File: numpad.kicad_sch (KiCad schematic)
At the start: 1 part, among them U1 ATmega328P-P

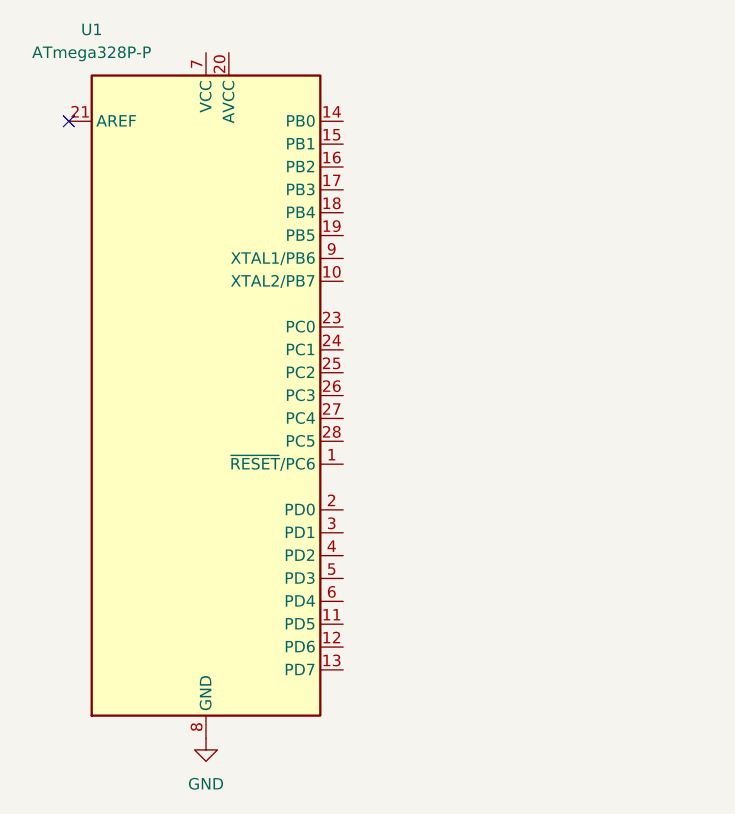
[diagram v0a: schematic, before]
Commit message: 스키메틱에 발진회로 추가
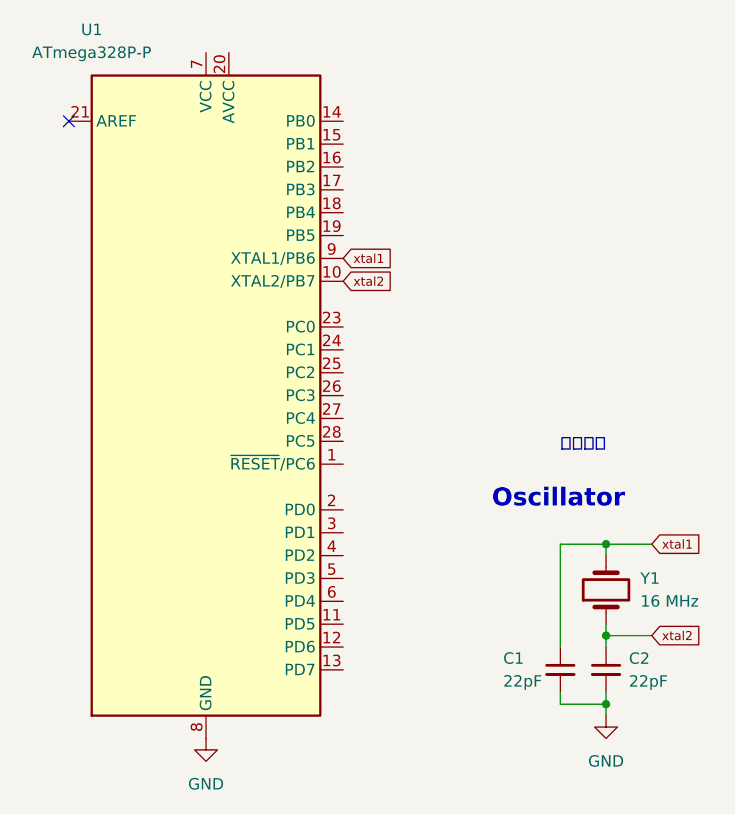
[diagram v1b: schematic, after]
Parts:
- added C1, C2: 22pF, symbol Device:C_Small
- added Y1: 16 MHz, symbol Device:Crystal
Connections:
- net GND: now also C1.2, C2.2
- net xtal2: now reaches U1.10 (XTAL2/PB7)
- net xtal2: now also C2.1, Y1.1
- net xtal1: now reaches U1.9 (XTAL1/PB6)
- net xtal1: now also C1.1, Y1.2
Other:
- note added: "Oscillator"
- note added: "발진회로"
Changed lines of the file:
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@@
 (kicad_sch (version 20211123) (generator eeschema)
   (paper "A4")
+  (junction (at 80.01 165.1) (diameter 0) (color 0 0 0 0)
+  )
+  (junction (at 80.01 182.88) (diameter 0) (color 0 0 0 0)
+  )
+  (junction (at 80.01 175.26) (diameter 0) (color 0 0 0 0)
+  )
   (no_connect (at 20.32 118.11))
+  (wire (pts (xy 85.09 165.1) (xy 80.01 165.1))
+    (stroke (width 0) (type default) (color 0 0 0 0))
+  )
+  (wire (pts (xy 74.93 181.61) (xy 74.93 182.88))
+    (stroke (width 0) (type default) (color 0 0 0 0))
+  )
+  (wire (pts (xy 80.01 165.1) (xy 80.01 166.37))
+    (stroke (width 0) (type default) (color 0 0 0 0))
+  )
+  (wire (pts (xy 80.01 175.26) (xy 85.09 175.26))
+    (stroke (width 0) (type default) (color 0 0 0 0))
+  )
+  (wire (pts (xy 80.01 175.26) (xy 80.01 176.53))
+    (stroke (width 0) (type default) (color 0 0 0 0))
+  )
+  (wire (pts (xy 80.01 182.88) (xy 80.01 184.15))
+    (stroke (width 0) (type default) (color 0 0 0 0))
+  )
+  (wire (pts (xy 74.93 165.1) (xy 74.93 176.53))
+    (stroke (width 0) (type default) (color 0 0 0 0))
+  )
+  (wire (pts (xy 80.01 175.26) (xy 80.01 173.99))
+    (stroke (width 0) (type default) (color 0 0 0 0))
+  )
+  (wire (pts (xy 74.93 165.1) (xy 80.01 165.1))
+    (stroke (width 0) (type default) (color 0 0 0 0))
+  )
+  (wire (pts (xy 80.01 181.61) (xy 80.01 182.88))
+    (stroke (width 0) (type default) (color 0 0 0 0))
+  )
+  (wire (pts (xy 74.93 182.88) (xy 80.01 182.88))
+    (stroke (width 0) (type default) (color 0 0 0 0))
+  )
+  (text "발진회로" (at 74.93 154.94 0)
+    (effects (font (size 1.27 1.27)) (justify left bottom))
+  )
+  (text "Oscillator" (at 67.31 161.29 0)
+    (effects (font (size 2 2) (thickness 0.4) bold) (justify left bottom))
+  )
+  (global_label "xtal2" (shape input) (at 50.8 135.89 0) (fields_autoplaced)
+    (effects (font (size 1 1)) (justify left))
+    (property "Intersheet References" "${INTERSHEET_REFS}" (id 0) (at 56.4619 135.8275 0)
+      (effects (font (size 1 1)) (justify left) hide)
+    )
+  )
+  (global_label "xtal2" (shape input) (at 85.09 175.26 0) (fields_autoplaced)
+    (effects (font (size 1 1)) (justify left))
+    (property "Intersheet References" "${INTERSHEET_REFS}" (id 0) (at 90.7519 175.1975 0)
+      (effects (font (size 1 1)) (justify left) hide)
+    )
+  )
+  (global_label "xtal1" (shape input) (at 85.09 165.1 0) (fields_autoplaced)
+    (effects (font (size 1 1)) (justify left))
+    (property "Intersheet References" "${INTERSHEET_REFS}" (id 0) (at 90.7519 165.0375 0)
+      (effects (font (size 1 1)) (justify left) hide)
+    )
+  )
+  (global_label "xtal1" (shape input) (at 50.8 133.35 0) (fields_autoplaced)
+    (effects (font (size 1 1)) (justify left))
+    (property "Intersheet References" "${INTERSHEET_REFS}" (id 0) (at 56.4619 133.2875 0)
+      (effects (font (size 1 1)) (justify left) hide)
+    )
+  )
+  (symbol (lib_id "Device:C_Small") (at 74.93 179.07 0) (unit 1)
+    (in_bom yes) (on_board yes)
+    (property "Reference" "C1" (id 0) (at 68.58 177.8 0)
+      (effects (font (size 1.27 1.27)) (justify left))
+    )
+    (property "Value" "22pF" (id 1) (at 68.58 180.34 0)
+      (effects (font (size 1.27 1.27)) (justify left))
+    )
+    (property "Footprint" "" (id 2) (at 74.93 179.07 0)
+      (effects (font (size 1.27 1.27)) hide)
+    )
+    (property "Datasheet" "~" (id 3) (at 74.93 179.07 0)
+      (effects (font (size 1.27 1.27)) hide)
+    )
+    (pin "1")
+    (pin "2")
+  )
   (symbol (lib_id "power:GND") (at 35.56 186.69 0) (unit 1)
     (in_bom yes) (on_board yes) (fields_autoplaced)
-    (property "Reference" "#PWR?" (id 0) (at 35.56 193.04 0)
+    (property "Reference" "#PWR01" (id 0) (at 35.56 193.04 0)
       (effects (font (size 1.27 1.27)) hide)
     )
@@
     )
     (property "Datasheet" "" (id 3) (at 35.56 186.69 0)
+      (effects (font (size 1.27 1.27)) hide)
+    )
+    (pin "1")
+  )
+  (symbol (lib_id "Device:C_Small") (at 80.01 179.07 0) (unit 1)
+    (in_bom yes) (on_board yes) (fields_autoplaced)
+    (property "Reference" "C2" (id 0) (at 82.55 177.8062 0)
+      (effects (font (size 1.27 1.27)) (justify left))
+    )
+    (property "Value" "22pF" (id 1) (at 82.55 180.3462 0)
+      (effects (font (size 1.27 1.27)) (justify left))
+    )
+    (property "Footprint" "" (id 2) (at 80.01 179.07 0)
+      (effects (font (size 1.27 1.27)) hide)
+    )
+    (property "Datasheet" "~" (id 3) (at 80.01 179.07 0)
+      (effects (font (size 1.27 1.27)) hide)
+    )
+    (pin "1")
+    (pin "2")
+  )
+  (symbol (lib_id "Device:Crystal") (at 80.01 170.18 90) (unit 1)
+    (in_bom yes) (on_board yes) (fields_autoplaced)
+    (property "Reference" "Y1" (id 0) (at 83.82 168.9099 90)
+      (effects (font (size 1.27 1.27)) (justify right))
+    )
+    (property "Value" "16 MHz" (id 1) (at 83.82 171.4499 90)
+      (effects (font (size 1.27 1.27)) (justify right))
+    )
+    (property "Footprint" "" (id 2) (at 80.01 170.18 0)
+      (effects (font (size 1.27 1.27)) hide)
+    )
+    (property "Datasheet" "~" (id 3) (at 80.01 170.18 0)
+      (effects (font (size 1.27 1.27)) hide)
+    )
+    (pin "1")
+    (pin "2")
+  )
+  (symbol (lib_id "power:GND") (at 80.01 184.15 0) (unit 1)
+    (in_bom yes) (on_board yes) (fields_autoplaced)
+    (property "Reference" "#PWR02" (id 0) (at 80.01 190.5 0)
+      (effects (font (size 1.27 1.27)) hide)
+    )
+    (property "Value" "GND" (id 1) (at 80.01 189.23 0))
+    (property "Footprint" "" (id 2) (at 80.01 184.15 0)
+      (effects (font (size 1.27 1.27)) hide)
+    )
+    (property "Datasheet" "" (id 3) (at 80.01 184.15 0)
       (effects (font (size 1.27 1.27)) hide)
     )
@@
   (symbol_instances
     (path "/2b550e1c-486d-4b24-938e-eef22acd13d2"
-      (reference "#PWR?") (unit 1) (value "GND") (footprint "")
+      (reference "#PWR01") (unit 1) (value "GND") (footprint "")
+    )
+    (path "/7e25601e-5f96-4a71-88fb-a810f9640b63"
+      (reference "#PWR02") (unit 1) (value "GND") (footprint "")
+    )
+    (path "/24216b76-9317-4acf-b8be-19f29f897fe8"
+      (reference "C1") (unit 1) (value "22pF") (footprint "")
+    )
+    (path "/483bbce9-f8cc-4652-8ad4-1fcda0c1c803"
+      (reference "C2") (unit 1) (value "22pF") (footprint "")
     )
     (path "/b9ae8c3c-44c9-4298-abbb-bb7043d095e8"
       (reference "U1") (unit 1) (value "ATmega328P-P") (footprint "Package_DIP:DIP-28_W7.62mm")
     )
-  )
+    (path "/54bd4ee0-7d16-4cdf-965e-99d5c8e4560b"
+      (reference "Y1") (unit 1) (value "16 MHz") (footprint "")
+    )
+  )
